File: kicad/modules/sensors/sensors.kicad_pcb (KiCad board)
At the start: 2 copper layers, 84.6 x 64 mm, 57 parts, among them J1 Bus_PCI_Express_x1, J4 Conn_01x02, J6 USB_C_Receptacle_USB2.0_16P, U2 RP2040, U4 W25Q128JVP, U5 BMP388, U8 BNO055, U9 MCP25625T-E/ML, X1 ABM8-272-T3, Y1 ABS07-32.768KHZ-T, Y2 X322516MLB4SI

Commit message: refine routing
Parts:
- added C92: 100n, Capacitor_SMD:C_0402_1005Metric, F.Cu at (145.2, 87.8)
- added C93: 100n, Capacitor_SMD:C_0402_1005Metric, F.Cu at (135.0, 87.9)
- moved C90 0.48 mm to (140.0, 82.5)
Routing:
- net +5V: track 37.0 -> 41.5 mm
- net +3.3V: track 175.4 -> 173.7 mm
- net CANSTBY: track 25.1 -> 24.5 mm
- net GND: vias 25 -> 46

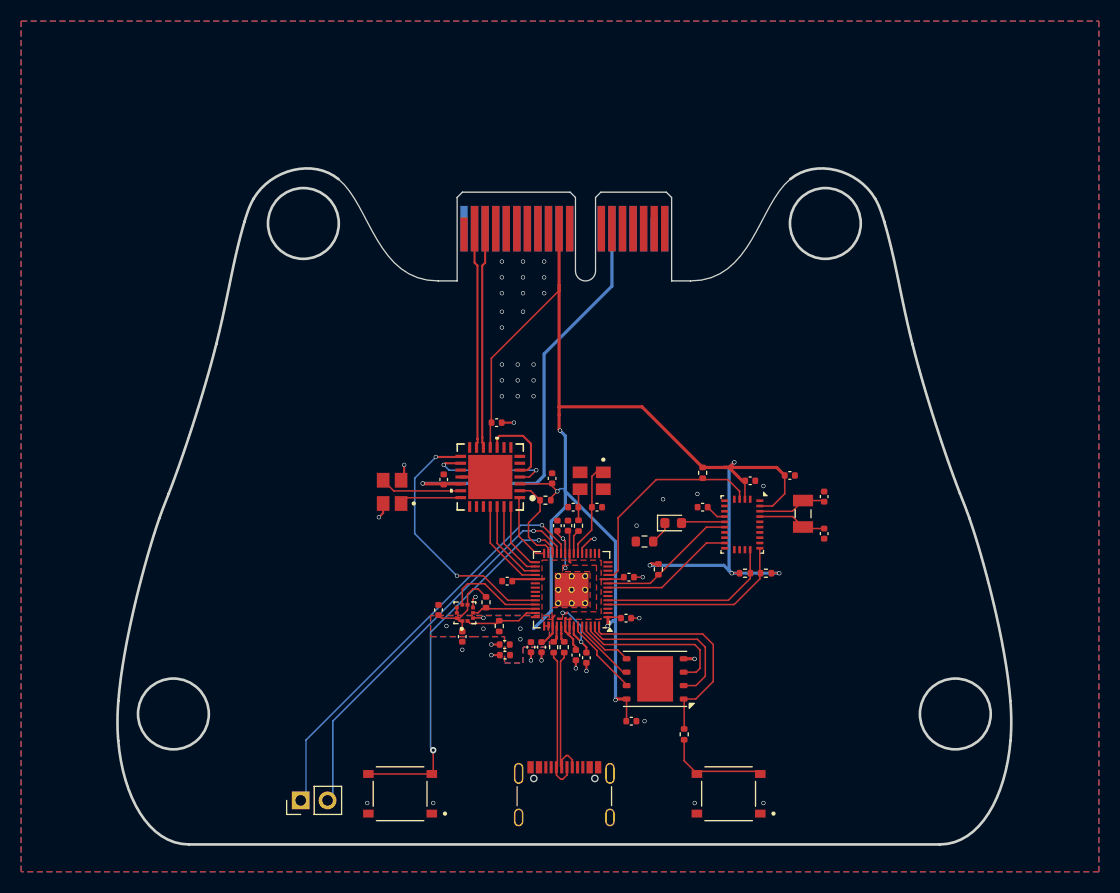
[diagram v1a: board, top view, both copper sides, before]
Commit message: finish diff pairs and planes
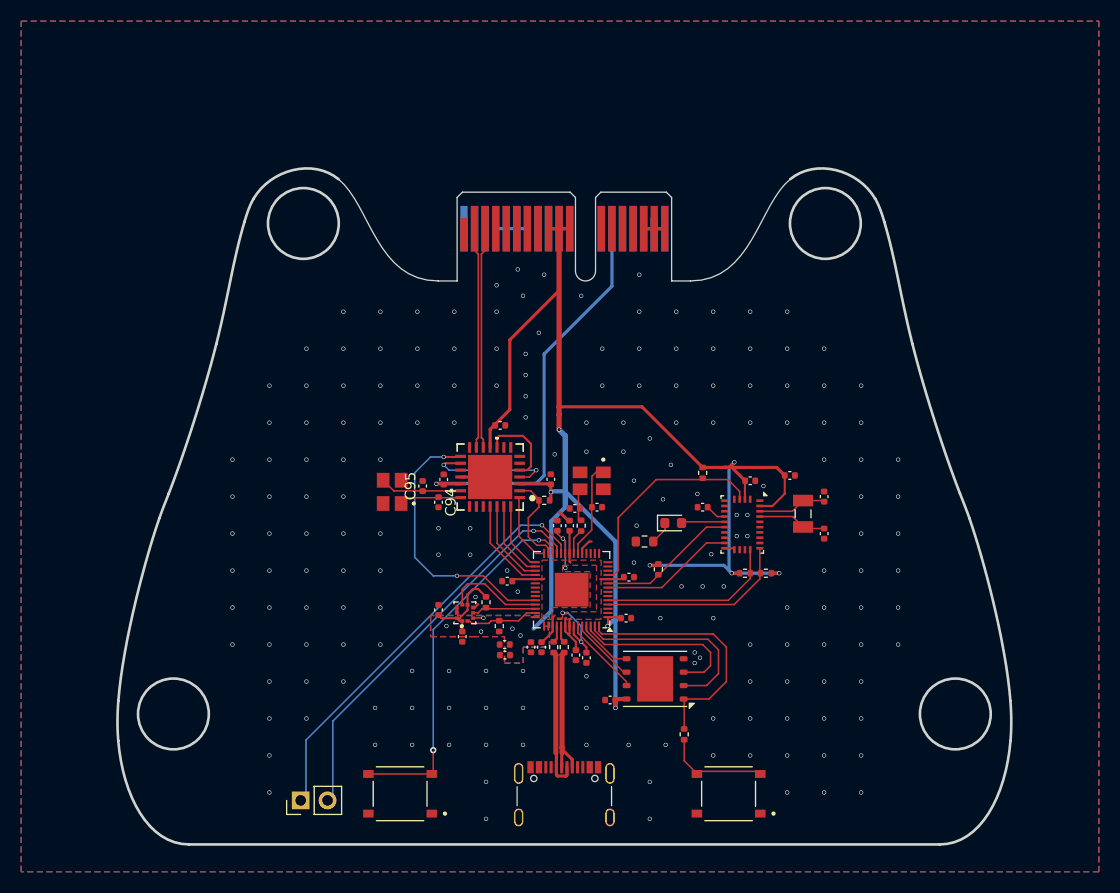
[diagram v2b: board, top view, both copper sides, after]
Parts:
- removed ? (x9): , 
- added C94: 22p, Capacitor_SMD:C_0402_1005Metric, F.Cu at (134.5, 90.0)
- added C95: 22p, Capacitor_SMD:C_0402_1005Metric, F.Cu at (133.0, 88.5)
- moved C40 2.83 mm to (150.8, 108.8), turned to 180 degrees
- moved C90 0.43 mm to (140.3, 82.8)
- moved R12 0.25 mm to (148.0, 92.2)
- moved C11 0.19 mm to (147.4, 90.6)
- moved C214 0.16 mm to (146.9, 92.3)
- moved C92 0.15 mm to (145.1, 87.9)
- moved R91 0.11 mm to (144.5, 89.9)
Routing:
- net GND: track 18.5 -> 12.6 mm, vias 46 -> 190
- net +7.4V: track 0.00 -> 4.00 mm
- net +3.3V: track 173.7 -> 176.9 mm
- net +5V: track 41.5 -> 38.9 mm
- net /QSPI_SS: track 21.7 -> 24.0 mm
- net /QSPI_SD1: track 16.7 -> 18.9 mm
- net /QSPI_SD2: track 15.0 -> 16.7 mm
- net CANSTBY: track 24.5 -> 26.1 mm
- net USB_D+: track 13.8 -> 13.2 mm

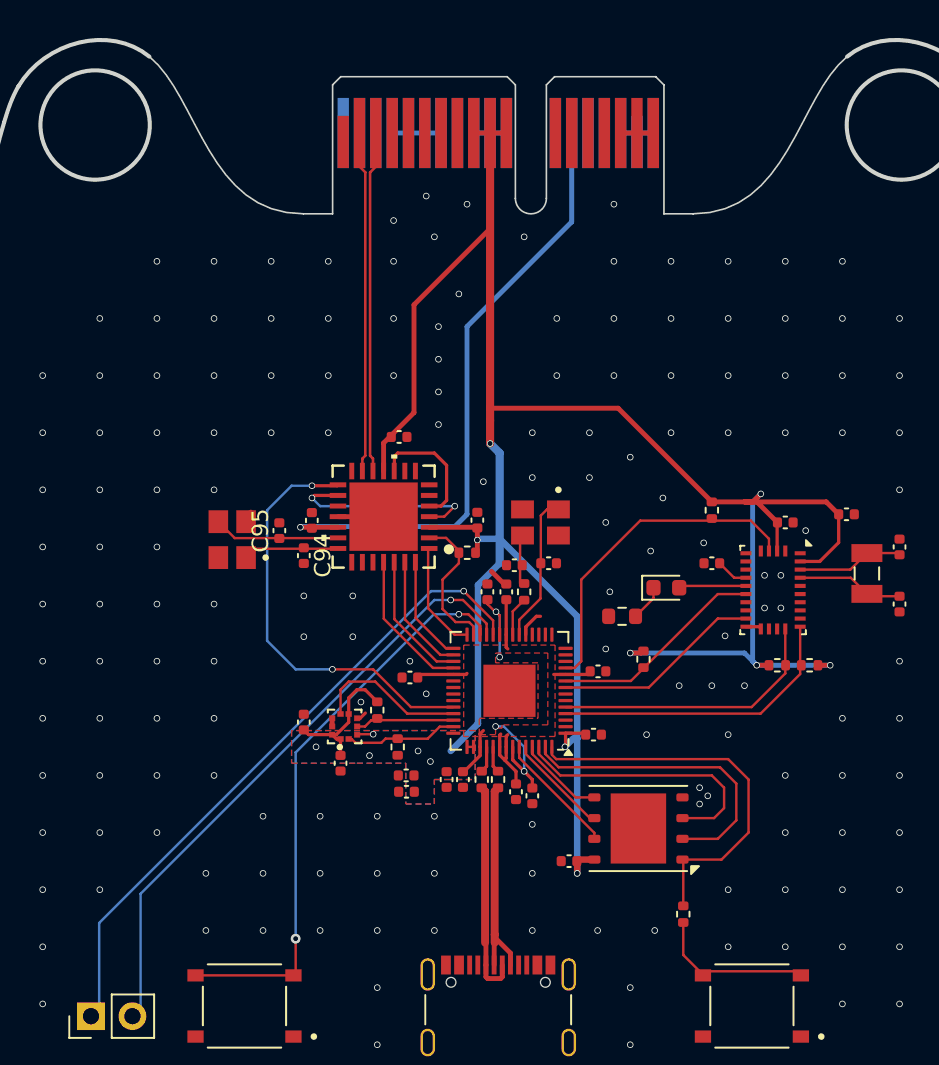
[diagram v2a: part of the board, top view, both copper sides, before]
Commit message: sensors: update PCIe pin nets, refine routing
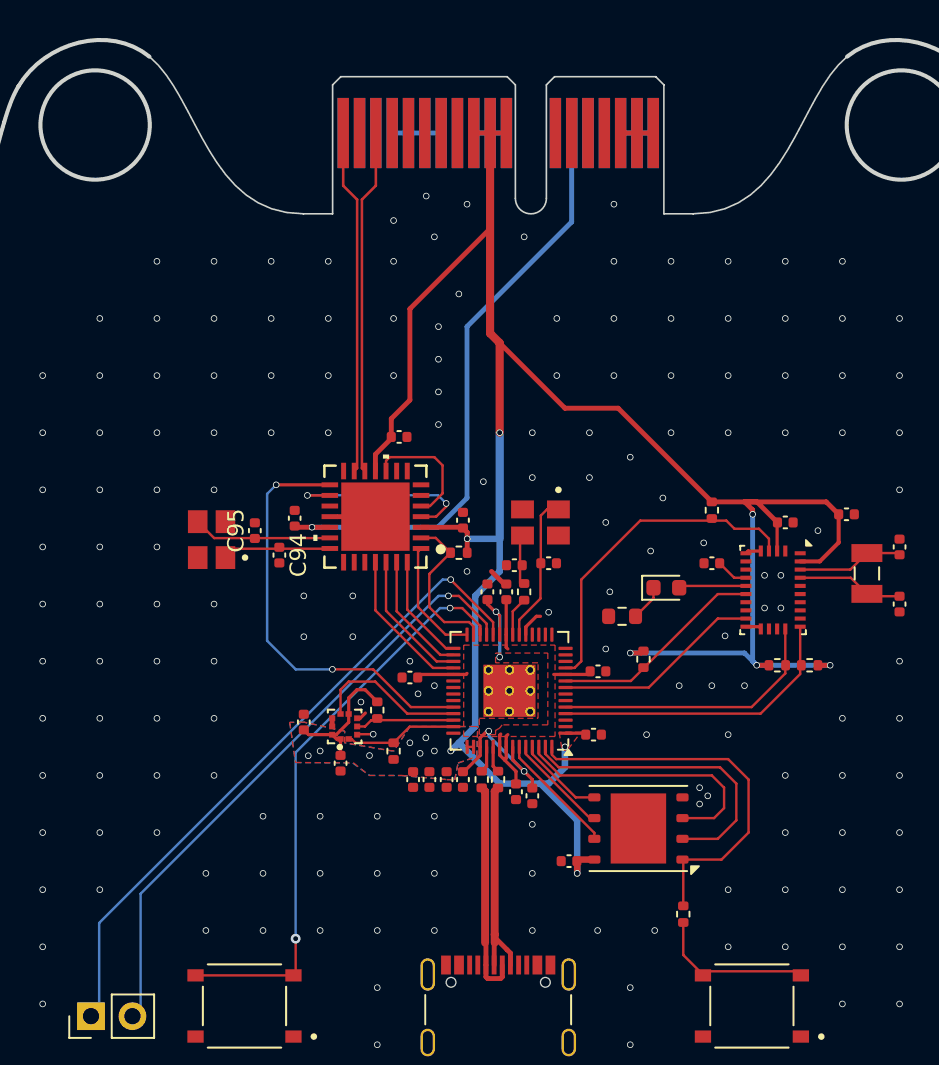
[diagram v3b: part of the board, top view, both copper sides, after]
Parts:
- added ?: , , F.Cu at (145.8, 98.3)
- added ?: , , F.Cu at (148.4, 98.3)
- added ?: , , F.Cu at (145.8, 99.6)
- added ?: , , F.Cu at (147.1, 98.3)
- added ?: , , F.Cu at (147.1, 99.6)
- added ?: , , F.Cu at (147.1, 97.0)
- added ?: , , F.Cu at (148.4, 99.6)
- added ?: , , F.Cu at (148.4, 97.0)
- added ?: , , F.Cu at (145.8, 97.0)
- moved C216 1.59 mm to (142.2, 103.7), turned to -90 degrees
- moved C94 1.50 mm to (133.0, 90.0)
- moved C95 1.50 mm to (131.5, 88.5)
- moved Y2 1.26 mm to (128.8, 89.1)
- moved C93 1.06 mm to (133.9, 87.7)
- moved C92 0.88 mm to (144.2, 87.9)
- moved R91 0.51 mm to (144.0, 89.9)
- moved U9 0.50 mm to (138.9, 87.6)
- moved C215 0.49 mm to (141.2, 103.7), turned to -90 degrees
- moved R222 0.36 mm to (140.0, 102.0)
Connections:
- J1 pad A1: GND -> CANP
- J1 pad A2: CANP -> unconnected-(J1-+12V-PadA2)
- J1 pad B2: CANP -> GND
- J1 pad B3: CANN -> GND
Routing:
- net +3.3V: track 176.9 -> 168.2 mm, vias 12 -> 16
- net +5V: track 38.9 -> 37.4 mm
- net OSC2: track 7.38 -> 8.64 mm
- net OSC1: track 5.49 -> 6.75 mm
- net CANRESET: track 8.98 -> 9.76 mm
- net rx: track 7.94 -> 7.24 mm
- net CS: track 6.75 -> 7.37 mm
- net GND: track 12.6 -> 13.1 mm, vias 190 -> 193
- net /SWCLK: track 39.6 -> 40.2 mm
